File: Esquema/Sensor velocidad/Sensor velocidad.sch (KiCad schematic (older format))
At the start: 49 parts

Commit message: Modifiqué error en puntos de medición de diodo y nomenclatura jumpers para sensor izquierdo y derecho
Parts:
- gave numbers to parts that had none: 7
- renumbered Jd3 to Jdr3
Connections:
- net Em_der: now also J?.1 (Pin_1)
- net Em_izq: now also J?.1 (Pin_1)
- net at JP?.2, Jde1.1, Jde2.1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: no longer J?.1 (Pin_1)
- net at JP?.2, Jie1.1, Jie2.1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: no longer J?.1 (Pin_1)
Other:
- moved on the sheet: J?
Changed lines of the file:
@@
 $EndComp
 $Comp
-L Device:Jumper_NO_Small Jd3
+L Device:Jumper_NO_Small Jdr3
 U 1 1 5EC7AFFE
 P 3650 1250
-F 0 "Jd3" V 3650 1298 50  0000 L CNN
+F 0 "Jdr3" V 3650 1298 50  0000 L CNN
 F 1 "Jumper_NO_Small" V 3695 1298 50  0001 L CNN
 F 2 "" H 3650 1250 50  0001 C CNN
@@
 L Connector:Conn_01x02_Male J?
 U 1 1 5EC9AF84
-P 850 1200
-F 0 "J?" H 958 1381 50  0000 C CNN
-F 1 "Conn_01x02_Male" H 958 1290 50  0000 C CNN
-F 2 "" H 850 1200 50  0001 C CNN
-F 3 "~" H 850 1200 50  0001 C CNN
-F 4 "Medición tensión en emisor" H 850 1200 50  0001 C CNN "Función"
-	1    850  1200
-	1    0    0    -1
-$EndComp
-Wire Wire Line
-	1050 1200 1450 1200
-Wire Wire Line
-	1450 1200 1450 1450
+P 750 2400
+F 0 "J?" H 858 2581 50  0000 C CNN
+F 1 "Conn_01x02_Male" H 858 2490 50  0000 C CNN
+F 2 "" H 750 2400 50  0001 C CNN
+F 3 "~" H 750 2400 50  0001 C CNN
+F 4 "Medición tensión en emisor" H 750 2400 50  0001 C CNN "Función"
+	1    750  2400
+	1    0    0    -1
+$EndComp
 $Comp
 L power:GND #PWR?
 U 1 1 5ECB0A65
-P 1050 1400
-F 0 "#PWR?" H 1050 1150 50  0001 C CNN
-F 1 "GND" H 1055 1227 50  0000 C CNN
-F 2 "" H 1050 1400 50  0001 C CNN
-F 3 "" H 1050 1400 50  0001 C CNN
-	1    1050 1400
-	1    0    0    -1
-$EndComp
-Wire Wire Line
-	1050 1400 1050 1300
+P 950 2600
+F 0 "#PWR?" H 950 2350 50  0001 C CNN
+F 1 "GND" H 955 2427 50  0000 C CNN
+F 2 "" H 950 2600 50  0001 C CNN
+F 3 "" H 950 2600 50  0001 C CNN
+	1    950  2600
+	1    0    0    -1
+$EndComp
+Wire Wire Line
+	950  2600 950  2500
 Wire Wire Line
 	3000 1650 3000 1850
@@
 $EndComp
 $Comp
-L Device:Jumper_NO_Small Jde?
+L Device:Jumper_NO_Small Jie1
 U 1 1 5ED56EE5
 P 1250 5350
-F 0 "Jde?" V 1250 5398 50  0000 L CNN
+F 0 "Jie1" V 1250 5398 50  0000 L CNN
 F 1 "Jumper_NO_Small" V 1295 5398 50  0001 L CNN
 F 2 "" H 1250 5350 50  0001 C CNN
@@
 $EndComp
 $Comp
-L Device:Jumper_NO_Small Jde?
+L Device:Jumper_NO_Small Jie2
 U 1 1 5ED56EF3
 P 1500 5350
-F 0 "Jde?" V 1500 5398 50  0000 L CNN
+F 0 "Jie2" V 1500 5398 50  0000 L CNN
 F 1 "Jumper_NO_Small" V 1545 5398 50  0001 L CNN
 F 2 "" H 1500 5350 50  0001 C CNN
@@
 $EndComp
 $Comp
-L Device:Jumper_NO_Small Jde?
+L Device:Jumper_NO_Small Jie3
 U 1 1 5ED56EFA
 P 1750 5350
-F 0 "Jde?" V 1750 5398 50  0000 L CNN
+F 0 "Jie3" V 1750 5398 50  0000 L CNN
 F 1 "Jumper_NO_Small" V 1795 5398 50  0001 L CNN
 F 2 "" H 1750 5350 50  0001 C CNN
@@
 $EndComp
 $Comp
-L Device:Jumper_NO_Small Jde?
+L Device:Jumper_NO_Small Jie4
 U 1 1 5ED56F01
 P 2000 5350
-F 0 "Jde?" V 2000 5398 50  0000 L CNN
+F 0 "Jie4" V 2000 5398 50  0000 L CNN
 F 1 "Jumper_NO_Small" V 2045 5398 50  0001 L CNN
 F 2 "" H 2000 5350 50  0001 C CNN
@@
 $EndComp
 $Comp
-L Device:Jumper_NO_Small Jdr?
+L Device:Jumper_NO_Small Jir1
 U 1 1 5ED56F37
 P 2900 4900
-F 0 "Jdr?" V 2900 4948 50  0000 L CNN
+F 0 "Jir1" V 2900 4948 50  0000 L CNN
 F 1 "Jumper_NO_Small" V 2945 4948 50  0001 L CNN
 F 2 "" H 2900 4900 50  0001 C CNN
@@
 $EndComp
 $Comp
-L Device:Jumper_NO_Small Jdr?
+L Device:Jumper_NO_Small Jir2
 U 1 1 5ED56F3E
 P 3300 4900
-F 0 "Jdr?" V 3300 4948 50  0000 L CNN
+F 0 "Jir2" V 3300 4948 50  0000 L CNN
 F 1 "Jumper_NO_Small" V 3345 4948 50  0001 L CNN
 F 2 "" H 3300 4900 50  0001 C CNN
@@
 $EndComp
 $Comp
-L Device:Jumper_NO_Small Jd?
+L Device:Jumper_NO_Small Jir3
 U 1 1 5ED56F45
 P 3700 4900
-F 0 "Jd?" V 3700 4948 50  0000 L CNN
+F 0 "Jir3" V 3700 4948 50  0000 L CNN
 F 1 "Jumper_NO_Small" V 3745 4948 50  0001 L CNN
 F 2 "" H 3700 4900 50  0001 C CNN
@@
 L Connector:Conn_01x02_Male J?
 U 1 1 5ED56F7D
-P 900 4850
-F 0 "J?" H 1008 5031 50  0000 C CNN
-F 1 "Conn_01x02_Male" H 1008 4940 50  0000 C CNN
-F 2 "" H 900 4850 50  0001 C CNN
-F 3 "~" H 900 4850 50  0001 C CNN
-F 4 "Medición tensión en emisor" H 900 4850 50  0001 C CNN "Función"
-	1    900  4850
-	1    0    0    -1
-$EndComp
-Wire Wire Line
-	1100 4850 1500 4850
-Wire Wire Line
-	1500 4850 1500 5100
+P 850 6050
+F 0 "J?" H 958 6231 50  0000 C CNN
+F 1 "Conn_01x02_Male" H 958 6140 50  0000 C CNN
+F 2 "" H 850 6050 50  0001 C CNN
+F 3 "~" H 850 6050 50  0001 C CNN
+F 4 "Medición tensión en emisor" H 850 6050 50  0001 C CNN "Función"
+	1    850  6050
+	1    0    0    -1
+$EndComp
 $Comp
 L power:GND #PWR?
 U 1 1 5ED56F85
-P 1100 5050
-F 0 "#PWR?" H 1100 4800 50  0001 C CNN
-F 1 "GND" H 1105 4877 50  0000 C CNN
-F 2 "" H 1100 5050 50  0001 C CNN
-F 3 "" H 1100 5050 50  0001 C CNN
-	1    1100 5050
-	1    0    0    -1
-$EndComp
-Wire Wire Line
-	1100 5050 1100 4950
+P 1050 6250
+F 0 "#PWR?" H 1050 6000 50  0001 C CNN
+F 1 "GND" H 1055 6077 50  0000 C CNN
+F 2 "" H 1050 6250 50  0001 C CNN
+F 3 "" H 1050 6250 50  0001 C CNN
+	1    1050 6250
+	1    0    0    -1
+$EndComp
+Wire Wire Line
+	1050 6250 1050 6150
 Wire Wire Line
 	3050 5300 3050 5500
@@
 Wire Wire Line
 	3950 7050 4150 7050
+Wire Wire Line
+	950  2400 1200 2400
+Connection ~ 1200 2400
+Wire Wire Line
+	1050 6050 1250 6050
+Connection ~ 1250 6050
 $EndSCHEMATC

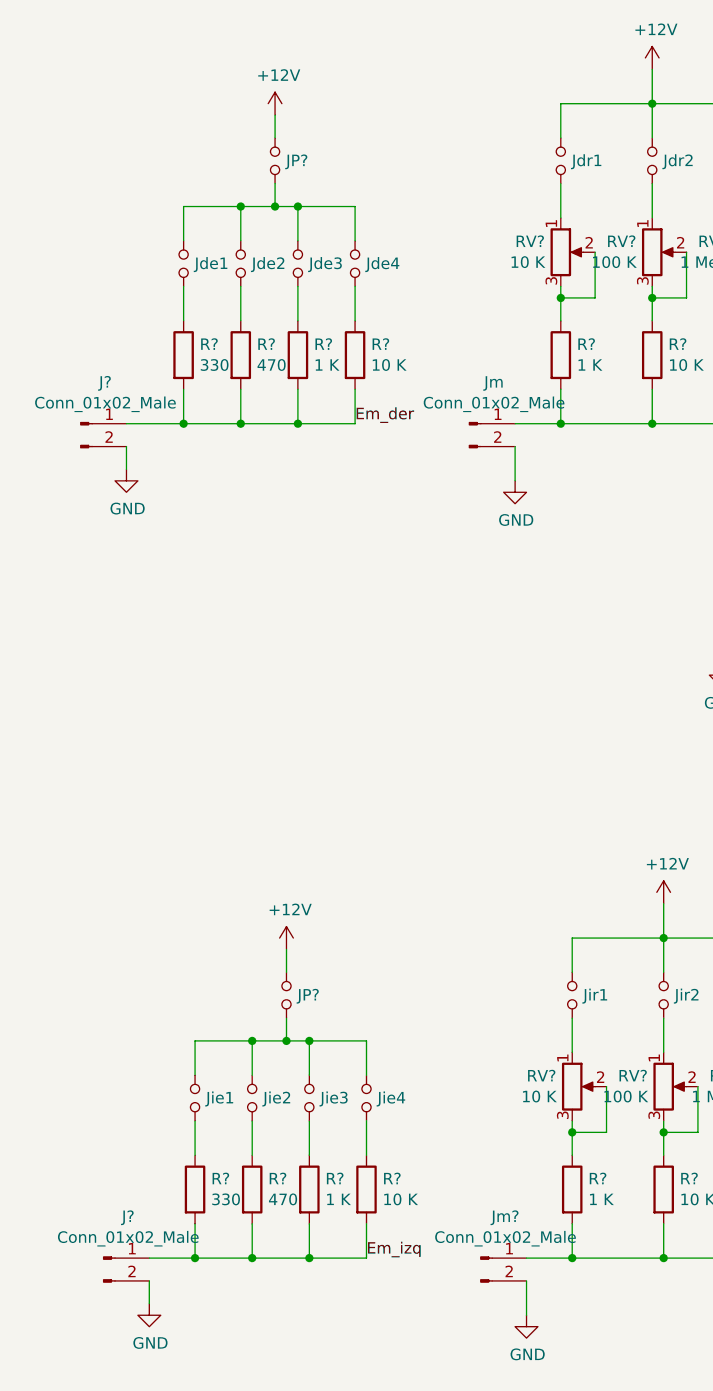
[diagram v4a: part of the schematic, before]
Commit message: Corregí nomenclatura de jumper de medición de receptor
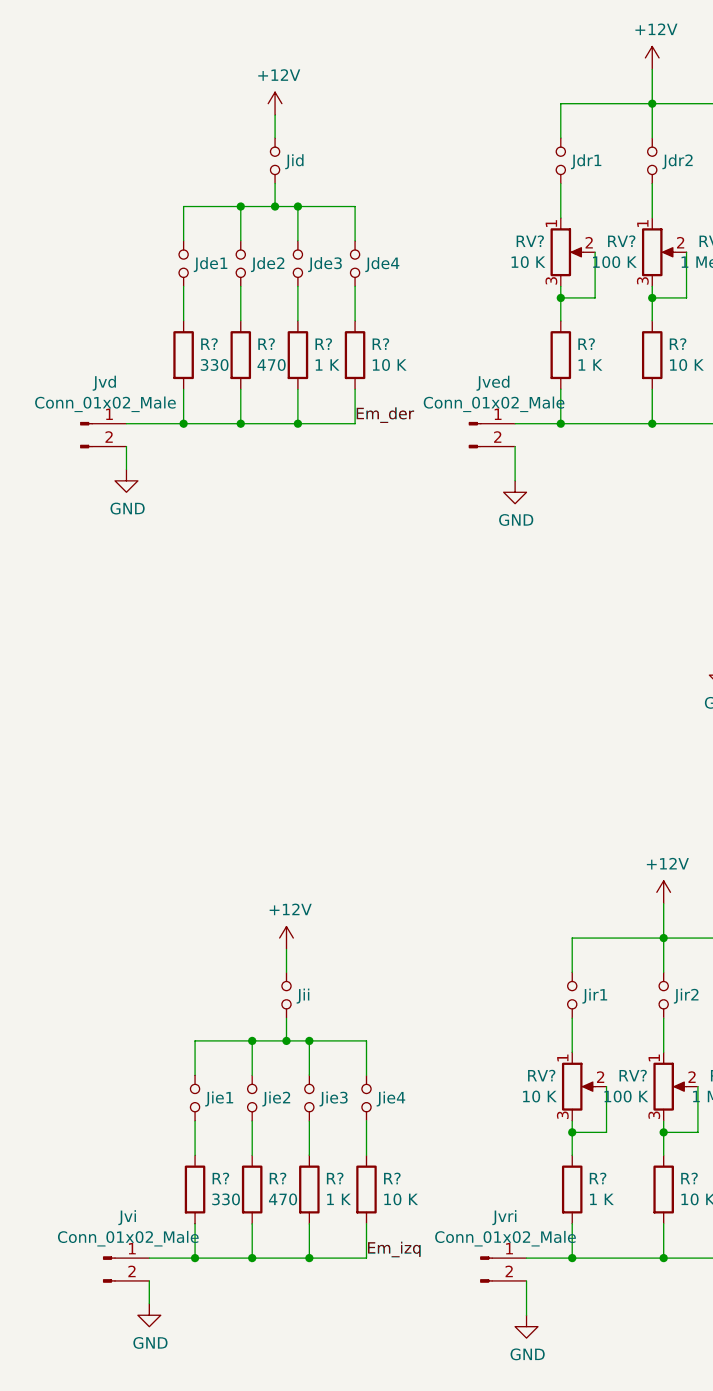
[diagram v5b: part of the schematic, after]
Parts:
- Jid: renamed from JP?; Función Medición corriente emisor -> Medición corriente emisor derecho
- Jii: renamed from JP?; Función Medición corriente emisor -> Medición corriente emisor izquierdo
- Jved: renamed from Jm; Función Medición de osciloscopio -> Medición de osciloscopio receptor derecho
- Jvri: renamed from Jm?; Función Medición de osciloscopio -> Medición de osciloscopio receptor izquierdo
- gave numbers to parts that had none: 2
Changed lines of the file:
@@
 	3650 1800 3650 1850
 $Comp
-L Device:Jumper_NO_Small JP?
+L Device:Jumper_NO_Small Jid
 U 1 1 5EC8EB0F
 P 1600 1250
-F 0 "JP?" V 1600 1298 50  0000 L CNN
+F 0 "Jid" V 1600 1298 50  0000 L CNN
 F 1 "Jumper_NO_Small" V 1645 1298 50  0001 L CNN
 F 2 "" H 1600 1250 50  0001 C CNN
 F 3 "~" H 1600 1250 50  0001 C CNN
-F 4 "Medición corriente emisor" V 1600 1250 50  0001 C CNN "Función"
+F 4 "Medición corriente emisor derecho" V 1600 1250 50  0001 C CNN "Función"
 	1    1600 1250
 	0    1    1    0
@@
 	1700 1450 1950 1450
 $Comp
-L Connector:Conn_01x02_Male J?
+L Connector:Conn_01x02_Male Jvd
 U 1 1 5EC9AF84
 P 750 2400
-F 0 "J?" H 858 2581 50  0000 C CNN
+F 0 "Jvd" H 858 2581 50  0000 C CNN
 F 1 "Conn_01x02_Male" H 858 2490 50  0000 C CNN
 F 2 "" H 750 2400 50  0001 C CNN
@@
 	3250 2400 3650 2400
 $Comp
-L Connector:Conn_01x02_Male Jm
+L Connector:Conn_01x02_Male Jved
 U 1 1 5ECC61EA
 P 2450 2400
-F 0 "Jm" H 2558 2581 50  0000 C CNN
+F 0 "Jved" H 2558 2581 50  0000 C CNN
 F 1 "Conn_01x02_Male" H 2558 2490 50  0000 C CNN
 F 2 "" H 2450 2400 50  0001 C CNN
 F 3 "~" H 2450 2400 50  0001 C CNN
-F 4 "Medición de osciloscopio" H 2450 2400 50  0001 C CNN "Función"
+F 4 "Medición de osciloscopio receptor derecho" H 2450 2400 50  0001 C CNN "Función"
 	1    2450 2400
 	1    0    0    -1
@@
 	3700 5450 3700 5500
 $Comp
-L Device:Jumper_NO_Small JP?
+L Device:Jumper_NO_Small Jii
 U 1 1 5ED56F69
 P 1650 4900
-F 0 "JP?" V 1650 4948 50  0000 L CNN
+F 0 "Jii" V 1650 4948 50  0000 L CNN
 F 1 "Jumper_NO_Small" V 1695 4948 50  0001 L CNN
 F 2 "" H 1650 4900 50  0001 C CNN
 F 3 "~" H 1650 4900 50  0001 C CNN
-F 4 "Medición corriente emisor" V 1650 4900 50  0001 C CNN "Función"
+F 4 "Medición corriente emisor izquierdo" V 1650 4900 50  0001 C CNN "Función"
 	1    1650 4900
 	0    1    1    0
@@
 	1750 5100 2000 5100
 $Comp
-L Connector:Conn_01x02_Male J?
+L Connector:Conn_01x02_Male Jvi
 U 1 1 5ED56F7D
 P 850 6050
-F 0 "J?" H 958 6231 50  0000 C CNN
+F 0 "Jvi" H 958 6231 50  0000 C CNN
 F 1 "Conn_01x02_Male" H 958 6140 50  0000 C CNN
 F 2 "" H 850 6050 50  0001 C CNN
@@
 	3300 6050 3700 6050
 $Comp
-L Connector:Conn_01x02_Male Jm?
+L Connector:Conn_01x02_Male Jvri
 U 1 1 5ED56FA8
 P 2500 6050
-F 0 "Jm?" H 2608 6231 50  0000 C CNN
+F 0 "Jvri" H 2608 6231 50  0000 C CNN
 F 1 "Conn_01x02_Male" H 2608 6140 50  0000 C CNN
 F 2 "" H 2500 6050 50  0001 C CNN
 F 3 "~" H 2500 6050 50  0001 C CNN
-F 4 "Medición de osciloscopio" H 2500 6050 50  0001 C CNN "Función"
+F 4 "Medición de osciloscopio receptor izquierdo" H 2500 6050 50  0001 C CNN "Función"
 	1    2500 6050
 	1    0    0    -1
